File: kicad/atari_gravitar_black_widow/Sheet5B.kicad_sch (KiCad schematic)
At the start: 28 parts

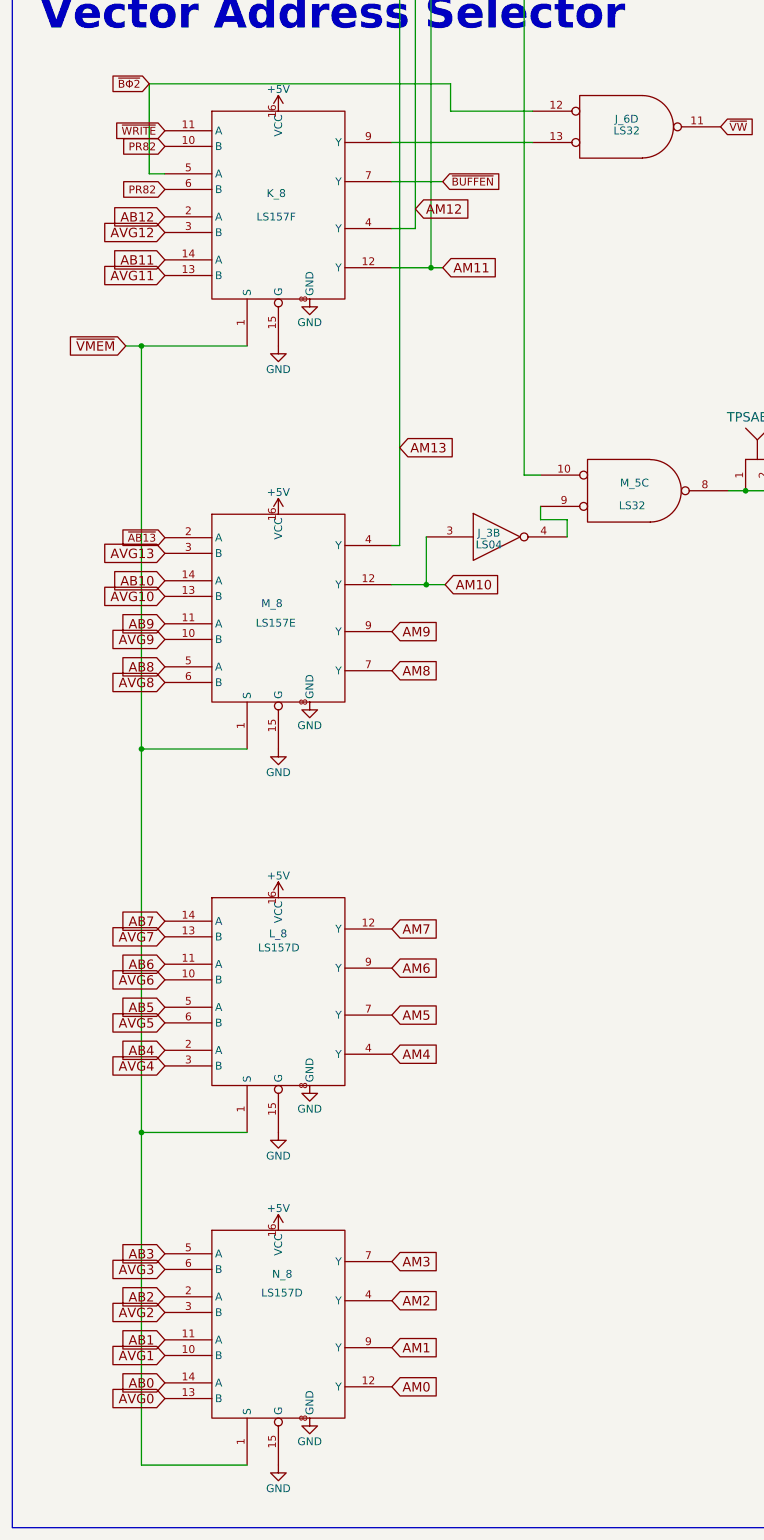
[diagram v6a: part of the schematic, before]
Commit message: Fixed all schematic warnings and fixed the edge cuts
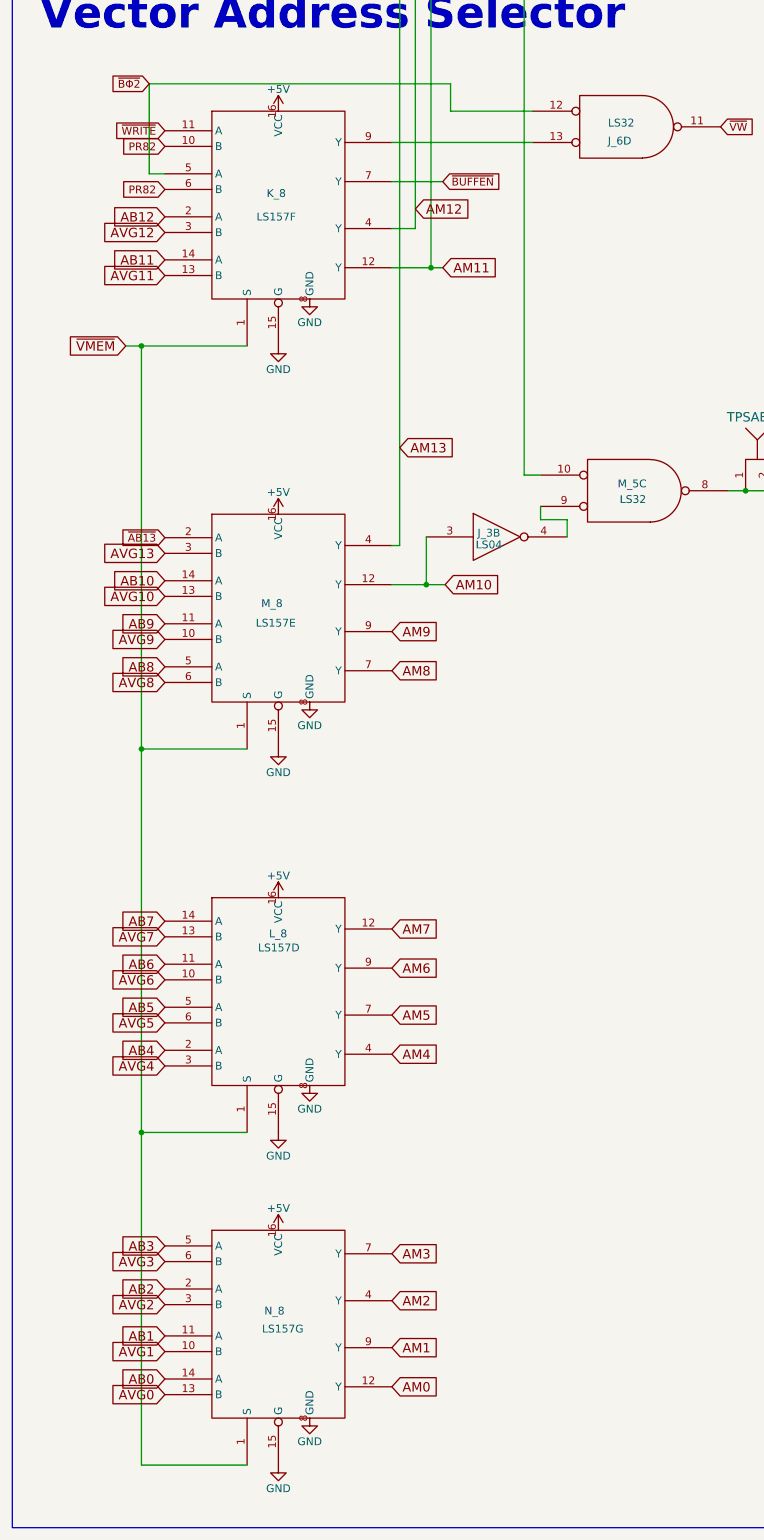
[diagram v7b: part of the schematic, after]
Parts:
- removed J_6, M_5: LS32, Star_Wars_Vector_PCB:DIP14, symbol atari_grav_bw:LS32
- removed N_8: LS157D, Star_Wars_Vector_PCB:DIP16, symbol atari_grav_bw:LS157D
- added J_6, M_5: LS32, Star_Wars_Vector_PCB:DIP14, symbol Star_Wars_Vector_PCB:LS32
- added N_8: LS157G, Star_Wars_Vector_PCB:DIP16, symbol atari_grav_bw:LS157G
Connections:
- net +5V: now also N_8.16 (VCC)
- net AB0: now also N_8.14 (A)
- net AB1: now also N_8.11 (A)
- net AB2: now also N_8.2 (A)
- net AB3: now also N_8.5 (A)
- net AM0: now also N_8.12 (Y)
- net AM1: now also N_8.9 (Y)
- net AM2: now also N_8.4 (Y)
- net AM3: now also N_8.7 (Y)
- net AVG0: now also N_8.13 (B)
- net AVG1: now also N_8.10 (B)
- net AVG2: now also N_8.3 (B)
- net AVG3: now also N_8.6 (B)
- net GND: now also N_8.15 (G), N_8.8 (GND)
- net ~{VMEM}: now also N_8.1 (S)

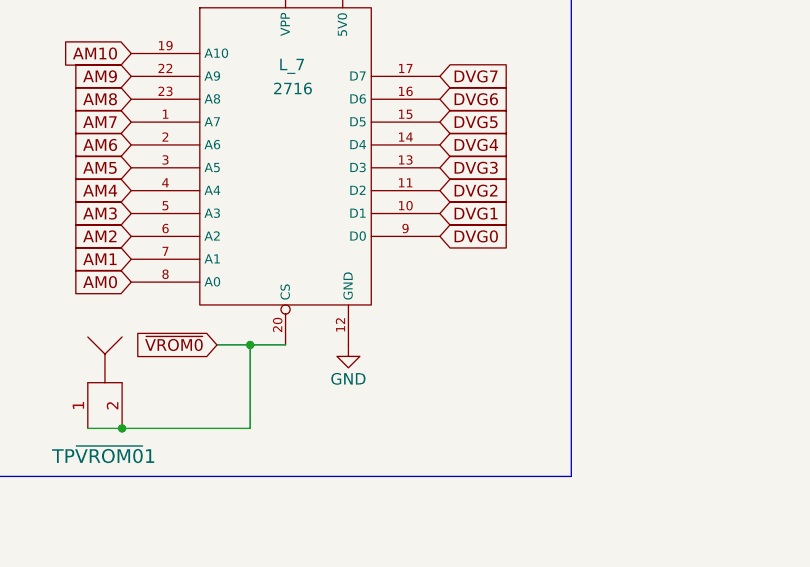
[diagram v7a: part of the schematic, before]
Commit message: Fixed all warning on PCB layout
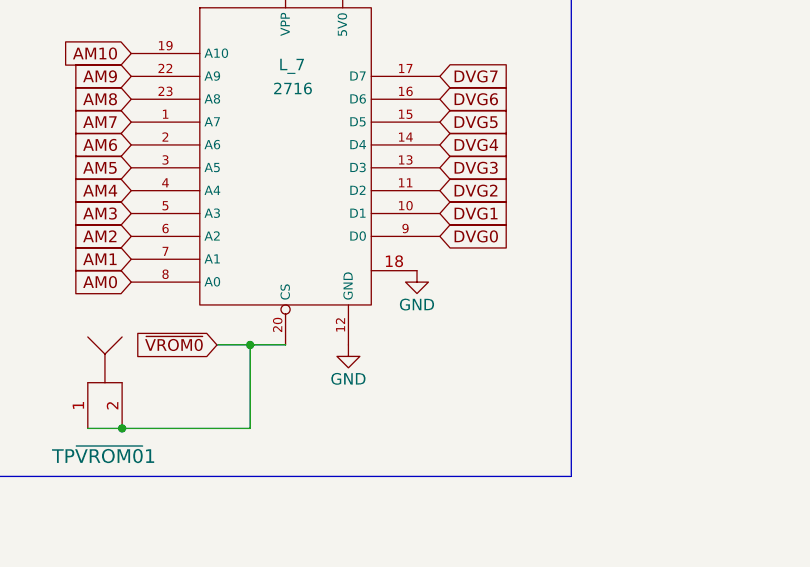
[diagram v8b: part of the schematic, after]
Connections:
- net GND: now also L_7.18
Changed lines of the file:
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@@
     (pin "8")
     (pin "9")
+    (pin "18")
   )
   (symbol (lib_id "power:GND") (at 203.2 91.44 0) (unit 1)
@@
       (effects (font (size 1.27 1.27)) hide)
     )
+    (pin "1")
+  )
+  (symbol (lib_id "power:GND") (at 401.32 83.185 0) (unit 1)
+    (in_bom yes) (on_board yes)
+    (property "Reference" "#PWR0195" (id 0) (at 401.32 89.535 0)
+      (effects (font (size 1.27 1.27)) hide)
+    )
+    (property "Value" "GND" (id 1) (at 401.32 86.995 0))
+    (property "Footprint" "" (id 2) (at 401.32 83.185 0)
+      (effects (font (size 1.27 1.27)) hide)
+    )
+    (property "Datasheet" "" (id 3) (at 401.32 83.185 0)
+      (effects (font (size 1.27 1.27)) hide)
+    )
